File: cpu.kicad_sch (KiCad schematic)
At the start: 26 parts, among them J1 FTSH-105-01-L-DV-K, J24 HTSW-103-07-G-S, U2 CC1312R1F3RGZR, Y2 OW7EL89CENUXK7YLC-48M

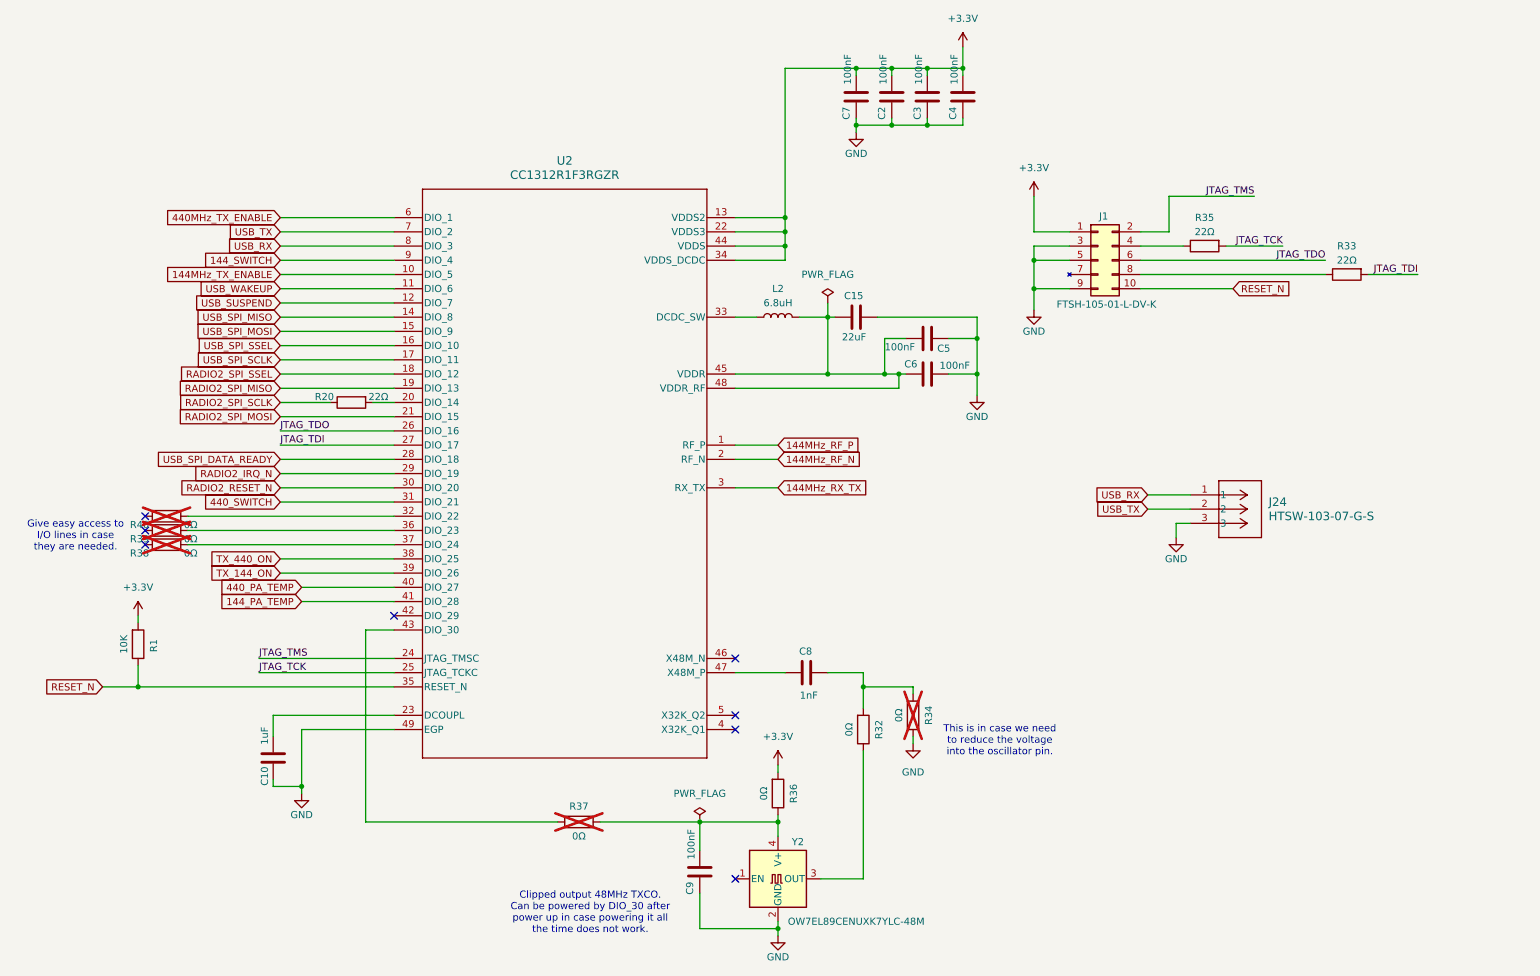
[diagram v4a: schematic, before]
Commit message: First start at reworking to get HDLC
Signed-off-by: Corey Minyard <corey@minyard.net>
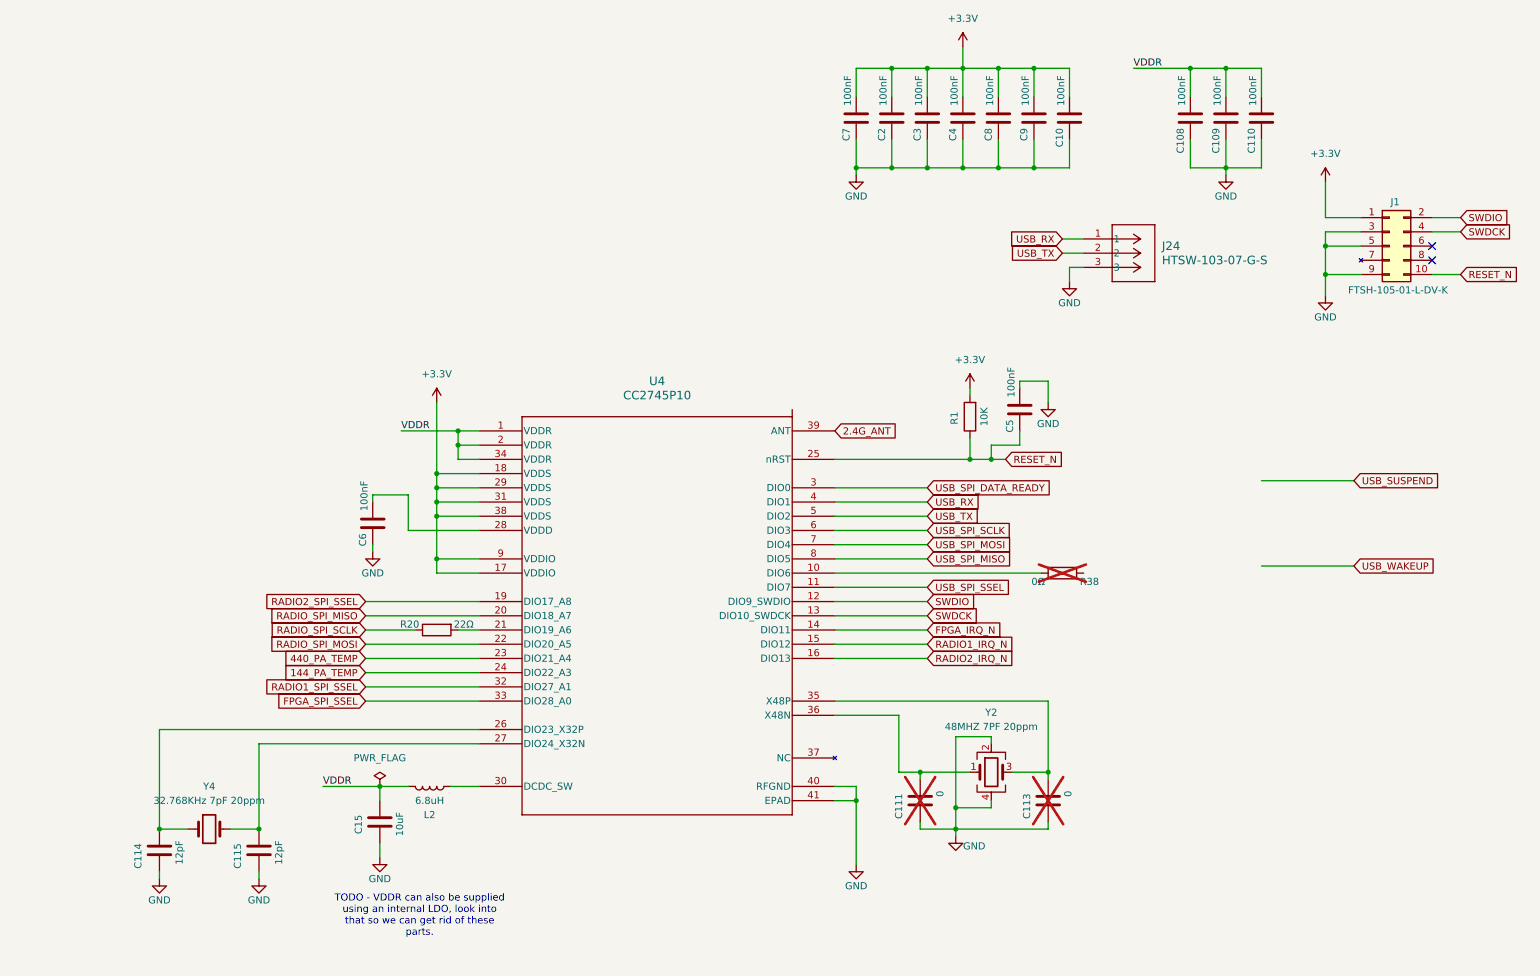
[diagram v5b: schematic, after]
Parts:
- removed R32, R34, R36, R37, R39, R40: 0Ω, Resistor_SMD:R_0402_1005Metric, symbol Device:R
- removed R33, R35: 22Ω, Resistor_SMD:R_0402_1005Metric, symbol Device:R
- removed U2: CC1312R1F3RGZR, footprints:RGZ0048A, symbol Local ICs:CC1312R1F3RGZR
- removed Y2: OW7EL89CENUXK7YLC-48M, Oscillator:Oscillator_SMD_SiT_PQFN-4Pin_2.0x1.6mm, symbol Local Passives:TXCO
- added C108, C109, C110: 100nF, Capacitor_SMD:C_0402_1005Metric_Pad0.74x0.62mm_HandSolder, symbol Device:C
- added C111, C113: 0, Capacitor_SMD:C_1206_3216Metric_Pad1.33x1.80mm_HandSolder, symbol Device:C
- added C114, C115: 12pF, Capacitor_SMD:C_1206_3216Metric_Pad1.33x1.80mm_HandSolder, symbol Device:C
- added U4: CC2745P10, footprints:RHA40_4P5X4P5, symbol ICs:CC2745P10
- added Y2: 48MHZ 7PF 20ppm, Crystal:Crystal_SMD_2016-4Pin_2.0x1.6mm, symbol Device:Crystal_GND24
- added Y4: 32.768KHz 7pF 20ppm, Crystal:Crystal_SMD_2012-2Pin_2.0x1.2mm, symbol Device:Crystal
- C10: value 1uF -> 100nF; footprint Capacitor_SMD:C_0603_1608Metric_Pad1.08x0.95mm_HandSolder -> Capacitor_SMD:C_0402_1005Metric_Pad0.74x0.62mm_HandSolder
- C15: value 22uF -> 10uF
- C8: value 1nF -> 100nF
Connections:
- net +3.3V: now also C10.2, C8.2, C9.2, U4.17 (VDDIO), U4.18 (VDDS), U4.29 (VDDS), U4.31 (VDDS), U4.38 (VDDS), U4.9 (VDDIO)
- net 144_PA_TEMP: now also U4.24 (DIO22_A3)
- net 440_PA_TEMP: now also U4.23 (DIO21_A4)
- net GND: now also C15.1, C5.2, C6.1, C8.1, C108.1, C109.1, C110.1, C111.1, C113.1, C114.1, C115.1, U4.40 (RFGND), U4.41 (EPAD), Y2.2, Y2.4; no longer C15.2, C5.1, C6.2
- net RADIO2_IRQ_N: now also U4.16 (DIO13)
- net RADIO2_SPI_SSEL: now also U4.19 (DIO17_A8)
- net RESET_N: now also C5.1, U4.25 (nRST)
- net USB_RX: now also U4.4 (DIO1)
- net USB_SPI_DATA_READY: now also U4.3 (DIO0)
- net USB_SPI_MISO: now also U4.8 (DIO5)
- net USB_SPI_MOSI: now also U4.7 (DIO4)
- net USB_SPI_SCLK: now also U4.6 (DIO3)
- net USB_SPI_SSEL: now also U4.11 (DIO7)
- net USB_TX: now also U4.5 (DIO2)
- net SWDCK: now reaches J1.4 (TCK)
- net SWDCK: now also U4.13 (DIO10_SWDCK)
- net at R38.1: now also U4.10 (DIO6)
- net at R20.2: now also U4.21 (DIO19_A6)
- net VDDR: now reaches L2.1
- net VDDR: now also C15.2, C108.2, C109.2, C110.2, U4.1 (VDDR), U4.2 (VDDR), U4.34 (VDDR)
- net JTAG_TDO: no longer names the net of J1.6 (TDO)
- net JTAG_TMS renamed SWDIO
- net SWDIO: now also U4.12 (DIO9_SWDIO)
- net RADIO2_SPI_SCLK renamed RADIO_SPI_SCLK
- new net: C111.2, U4.36 (X48N), Y2.1
- new net: C113.2, U4.35 (X48P), Y2.3
- new net: C115.2, U4.27 (DIO24_X32N), Y4.2
- new net: C6.2, U4.28 (VDDD)
- new net: C114.2, U4.26 (DIO23_X32P), Y4.1
- new net: L2.2, U4.30 (DCDC_SW)
- new net 2.4G_ANT: U4.39 (ANT)
- new net FPGA_IRQ_N: U4.14 (DIO11)
- new net FPGA_SPI_SSEL: U4.33 (DIO28_A0)
- new net RADIO1_IRQ_N: U4.15 (DIO12)
- new net RADIO1_SPI_SSEL: U4.32 (DIO27_A1)
- new net RADIO_SPI_MISO: U4.20 (DIO18_A7)
- new net RADIO_SPI_MOSI: U4.22 (DIO20_A5)
- no-connect marks 8 -> 2
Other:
- note added: "TODO - VDDR can also be supplied using an internal LDO, look into that so we can get rid of these parts."
- note removed: "Clipped output 48MHz TXCO. Can be powered by DIO_30 after power up in case powering it all the time does not work."
- note removed: "Give easy access to I/O lines in case they are needed."
- note removed: "This is in case we need to reduce the voltage into the oscillator pin."
- moved on the sheet: C15, C2, C3, C4, C7, J1, J24, L2, R1, R20, R38

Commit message: More re-layout for the new design
Signed-off-by: Corey Minyard <corey@minyard.net>
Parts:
- removed C10: 100nF, Capacitor_SMD:C_0402_1005Metric_Pad0.74x0.62mm_HandSolder, symbol Device:C
- removed R38: 0Ω, Resistor_SMD:R_0402_1005Metric, symbol Device:R
- C111, C113, C114, C115: footprint Capacitor_SMD:C_1206_3216Metric_Pad1.33x1.80mm_HandSolder -> Capacitor_SMD:C_0402_1005Metric_Pad0.74x0.62mm_HandSolder
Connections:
- net RADIO1_IRQ_N is gone; now on net USB_WAKEUP: U4.15 (DIO12)
- net 144_PA_TEMP: now also U4.23 (DIO21_A4); no longer U4.24 (DIO22_A3)
- net 440_PA_TEMP: now also U4.24 (DIO22_A3); no longer U4.23 (DIO21_A4)
- net FPGA_SPI_SSEL: now also U4.32 (DIO27_A1); no longer U4.33 (DIO28_A0)
- net RADIO1_SPI_SSEL: now also U4.33 (DIO28_A0); no longer U4.32 (DIO27_A1)
- net RADIO_SPI_MOSI: now also U4.21 (DIO19_A6); no longer U4.22 (DIO20_A5)
- net USB_SUSPEND: now also U4.10 (DIO6)
- net at R20.2: now also U4.22 (DIO20_A5); no longer U4.21 (DIO19_A6)
- net FPGA_IRQ_N renamed FPGA_CDONE/IRQ_N
- net RADIO2_IRQ_N renamed FPGA_RESET_N
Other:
- moved on the sheet: R20

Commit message: Finish initial layet
Signed-off-by: Corey Minyard <corey@minyard.net>
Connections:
- net USB_SPI_DATA_READY: no longer names the net of U4.3 (DIO0)
- no-connect marks 2 -> 3
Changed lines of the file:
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@@
+	)
+	(no_connect
+		(at 157.48 100.33)
 	)
 	(no_connect
@@
 		(pts
 			(xy 49.53 161.29) (xy 54.61 161.29)
-		)
-		(stroke
-			(width 0)
-			(type default)
-		)
-	)
-	(wire
-		(pts
-			(xy 173.99 100.33) (xy 157.48 100.33)
 		)
 		(stroke
@@
 				(hide yes)
 			)
-		)
-	)
-	(global_label "USB_SPI_DATA_READY"
-		(shape input)
-		(at 173.99 100.33 0)
-		(fields_autoplaced yes)
-		(effects
-			(font
-				(size 1.27 1.27)
-			)
-			(justify left)
-		)
-		(property "Intersheetrefs" "${INTERSHEET_REFS}"
-			(at 197.0533 100.33 0)
-			(effects
-				(font
-					(size 1.27 1.27)
-				)
-				(justify left)
-				(hide yes)
-			)

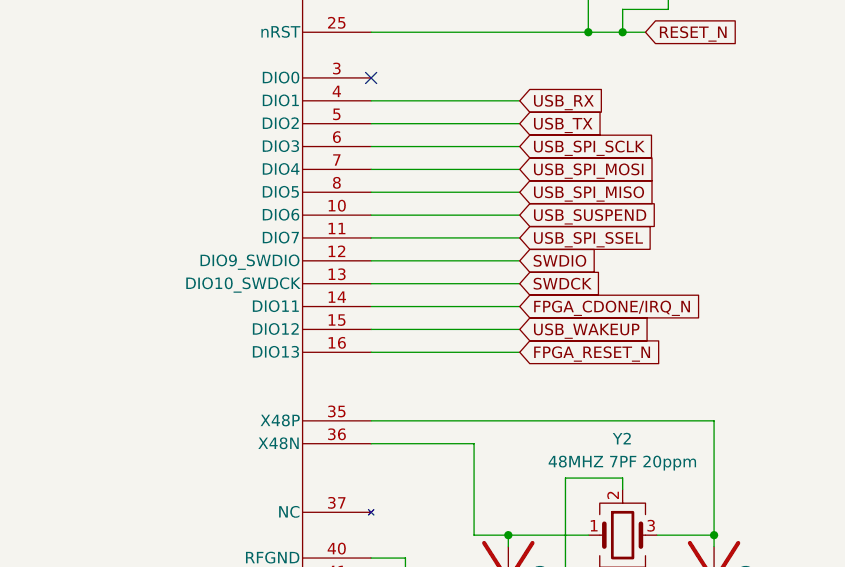
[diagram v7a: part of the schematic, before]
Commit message: Fix CC2745 layout
Some pins were wrong.

Also clean up a lot of layout issues caused by setting the clearance so
low to get the FPGA to route.  Set it back to normal constraints and
mark all the FPGA exclusions.

Signed-off-by: Corey Minyard <corey@minyard.net>
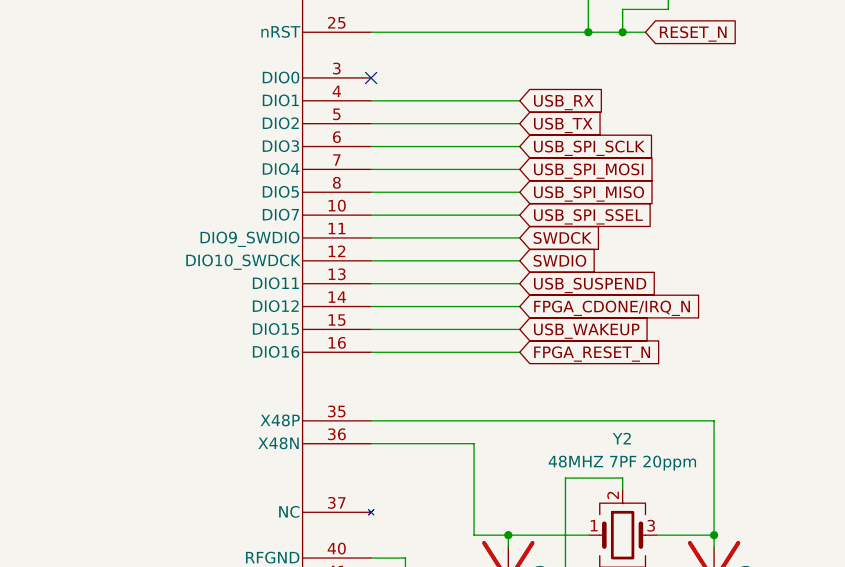
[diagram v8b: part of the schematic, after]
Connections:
- net SWDCK: now also U4.11 (DIO9_SWDIO); no longer U4.13 (DIO10_SWDCK)
- net USB_SPI_SSEL: now also U4.10 (DIO7); no longer U4.11 (DIO7)
- net USB_SUSPEND: now also U4.13 (DIO11); no longer U4.10 (DIO6)
